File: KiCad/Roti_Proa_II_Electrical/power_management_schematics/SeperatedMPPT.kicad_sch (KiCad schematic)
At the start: 17 parts

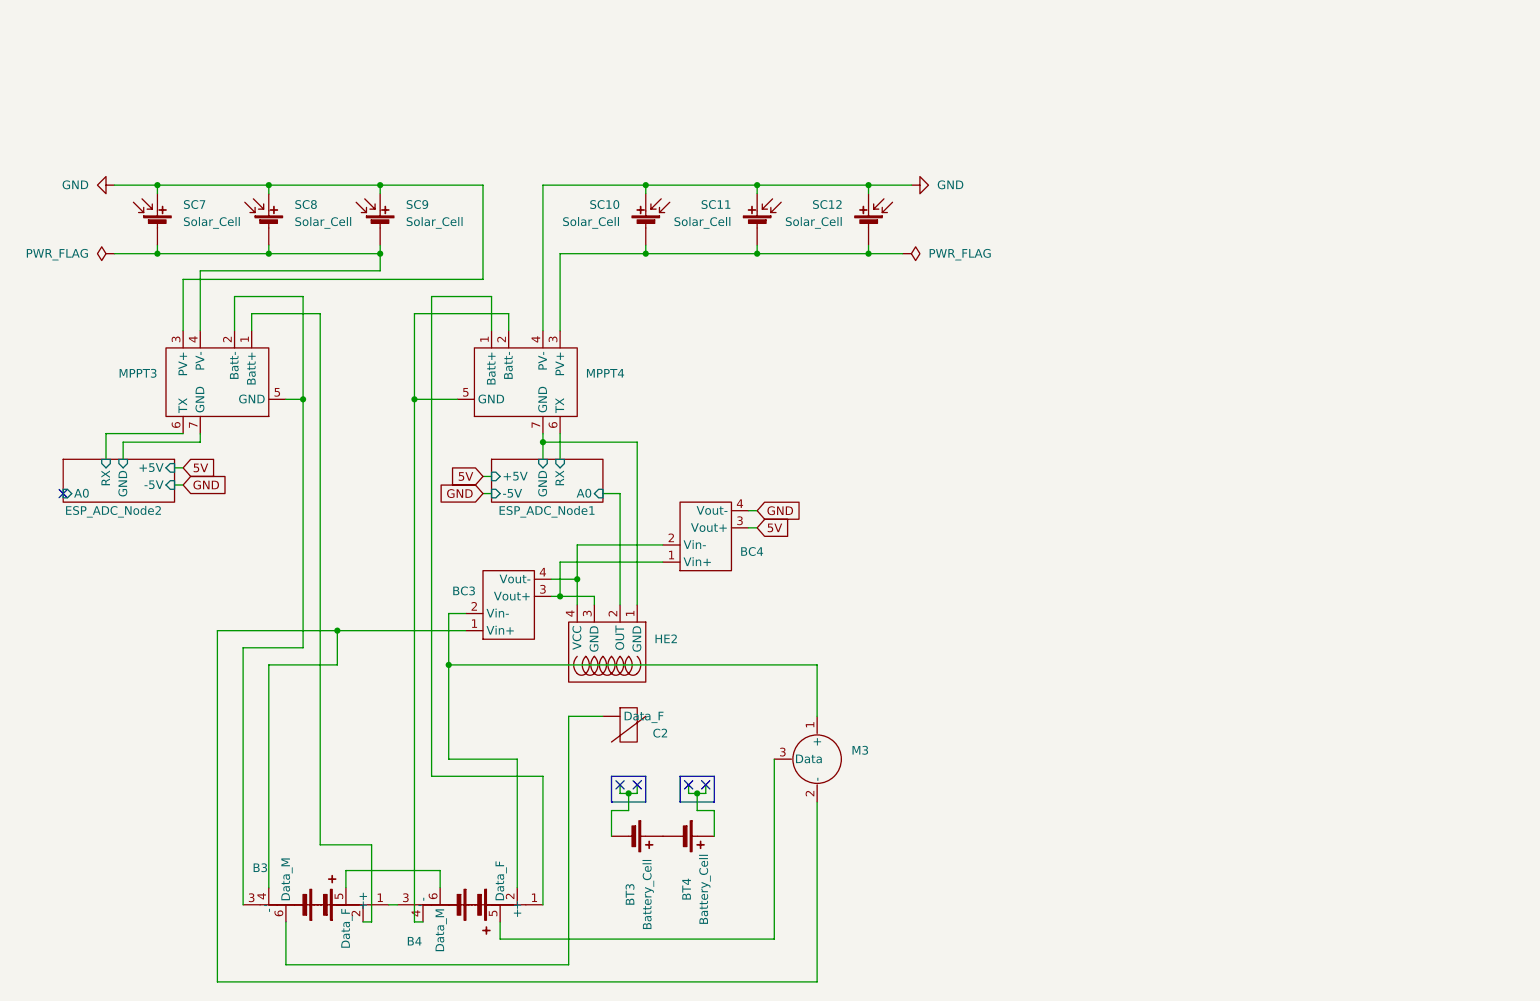
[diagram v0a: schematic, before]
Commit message: Complete MPPT+HE reading
Reading works for arduino and esp8266
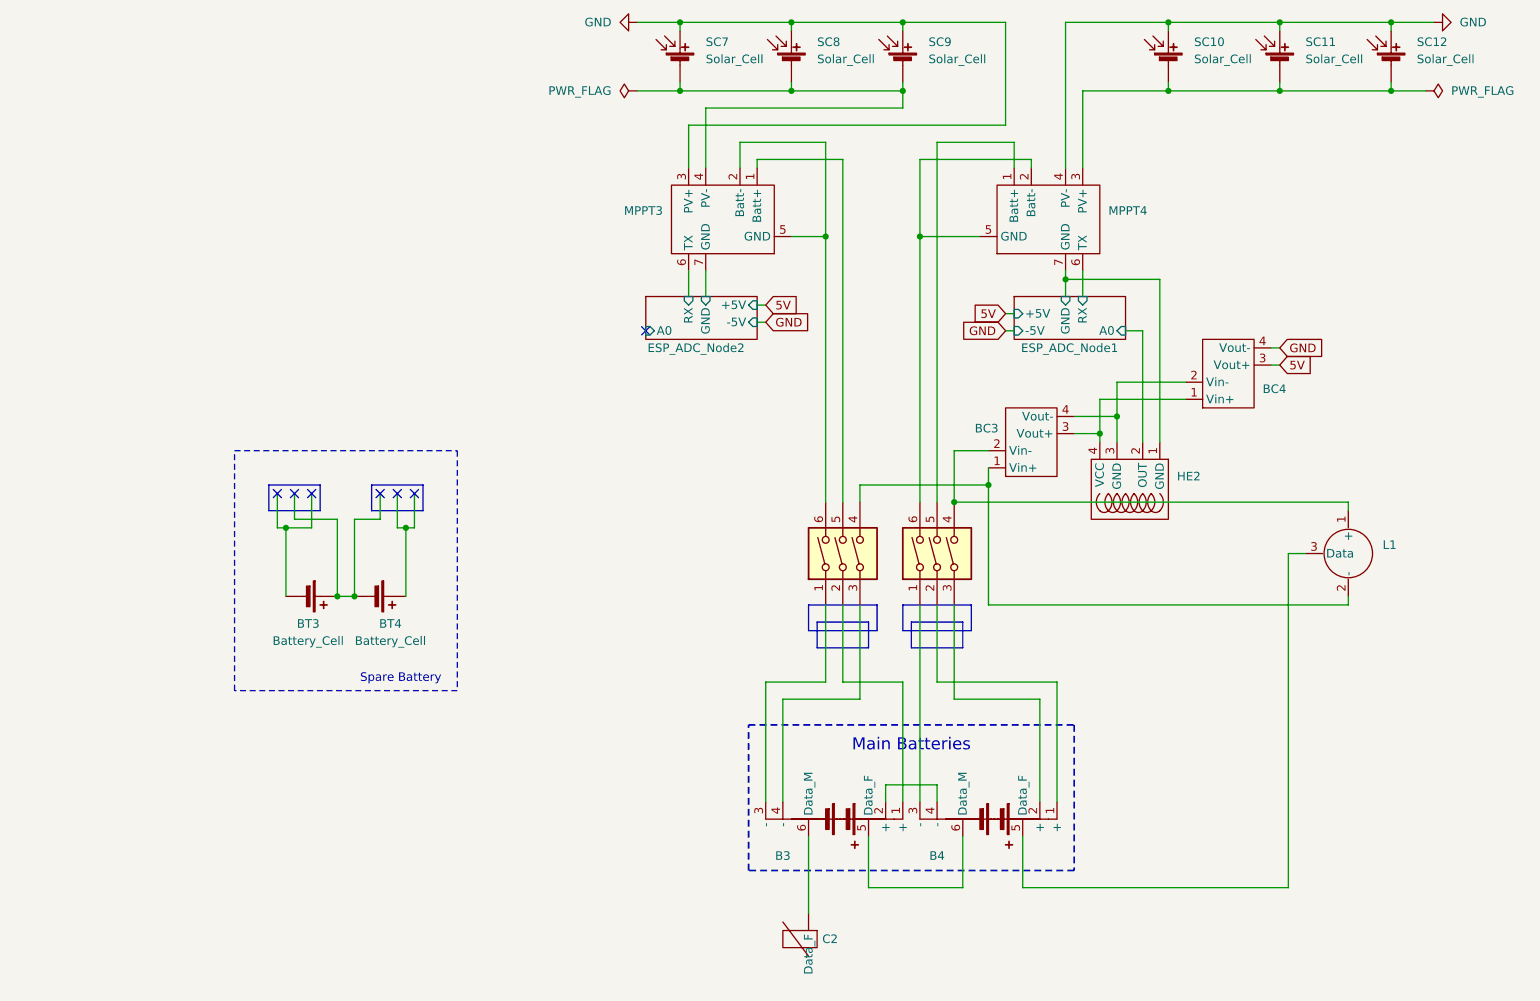
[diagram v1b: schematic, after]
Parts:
- removed M3: ~, symbol Proa2_v2:Motor
- added L1: ~, symbol Proa2_v2:Motor
- added SW3, SW4: SW_DIP_x03, symbol Switch:SW_DIP_x03
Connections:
- net at B3.1 (+): now also SW3.2; no longer B4.3 (-)
- net at B3.2 (+): now also B4.4 (-); no longer MPPT3.1 (Batt+)
- net at MPPT3.2 (Batt-), MPPT3.5 (GND): now also SW3.6; no longer B3.3 (-)
- net at B3.4 (-): now also SW3.3; no longer BC3.1 (Vin+)
- net at MPPT4.1 (Batt+): now also SW4.5; no longer B4.1 (+)
- net at MPPT4.2 (Batt-), MPPT4.5 (GND): now also SW4.6; no longer B4.4 (-)
- net at BC3.3 (Vout+), BC4.1 (Vin+): now also HE2.4 (VCC); no longer HE2.3 (GND)
- net at BC3.4 (Vout-), BC4.2 (Vin-): now also HE2.3 (GND); no longer HE2.4 (VCC)
- net at B4.2 (+): now also SW4.3; no longer BC3.2 (Vin-)
- net at B4.5 (Data_F): now also L1.3 (Data)
- new net: B3.3 (-), SW3.1
- new net: B4.3 (-), SW4.1
- new net: B4.1 (+), SW4.2
- new net: BC3.2 (Vin-), L1.1 (+), SW4.4
- new net: BC3.1 (Vin+), L1.2 (-), SW3.4
- new net: MPPT3.1 (Batt+), SW3.5
- no-connect marks 5 -> 7
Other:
- note added: "Main Batteries"
- note added: "Spare Battery"
- moved on the sheet: BC3, BC4, C2, HE2, MPPT3, MPPT4, SC7, SC8, SC9
